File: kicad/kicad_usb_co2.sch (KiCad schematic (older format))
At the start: 7 parts, among them SW1 SW_SPDT, SW2 SW_SPDT, U1 MH-Z19B, U2 SeeeduinoXIAO, U3 MH-Z14A

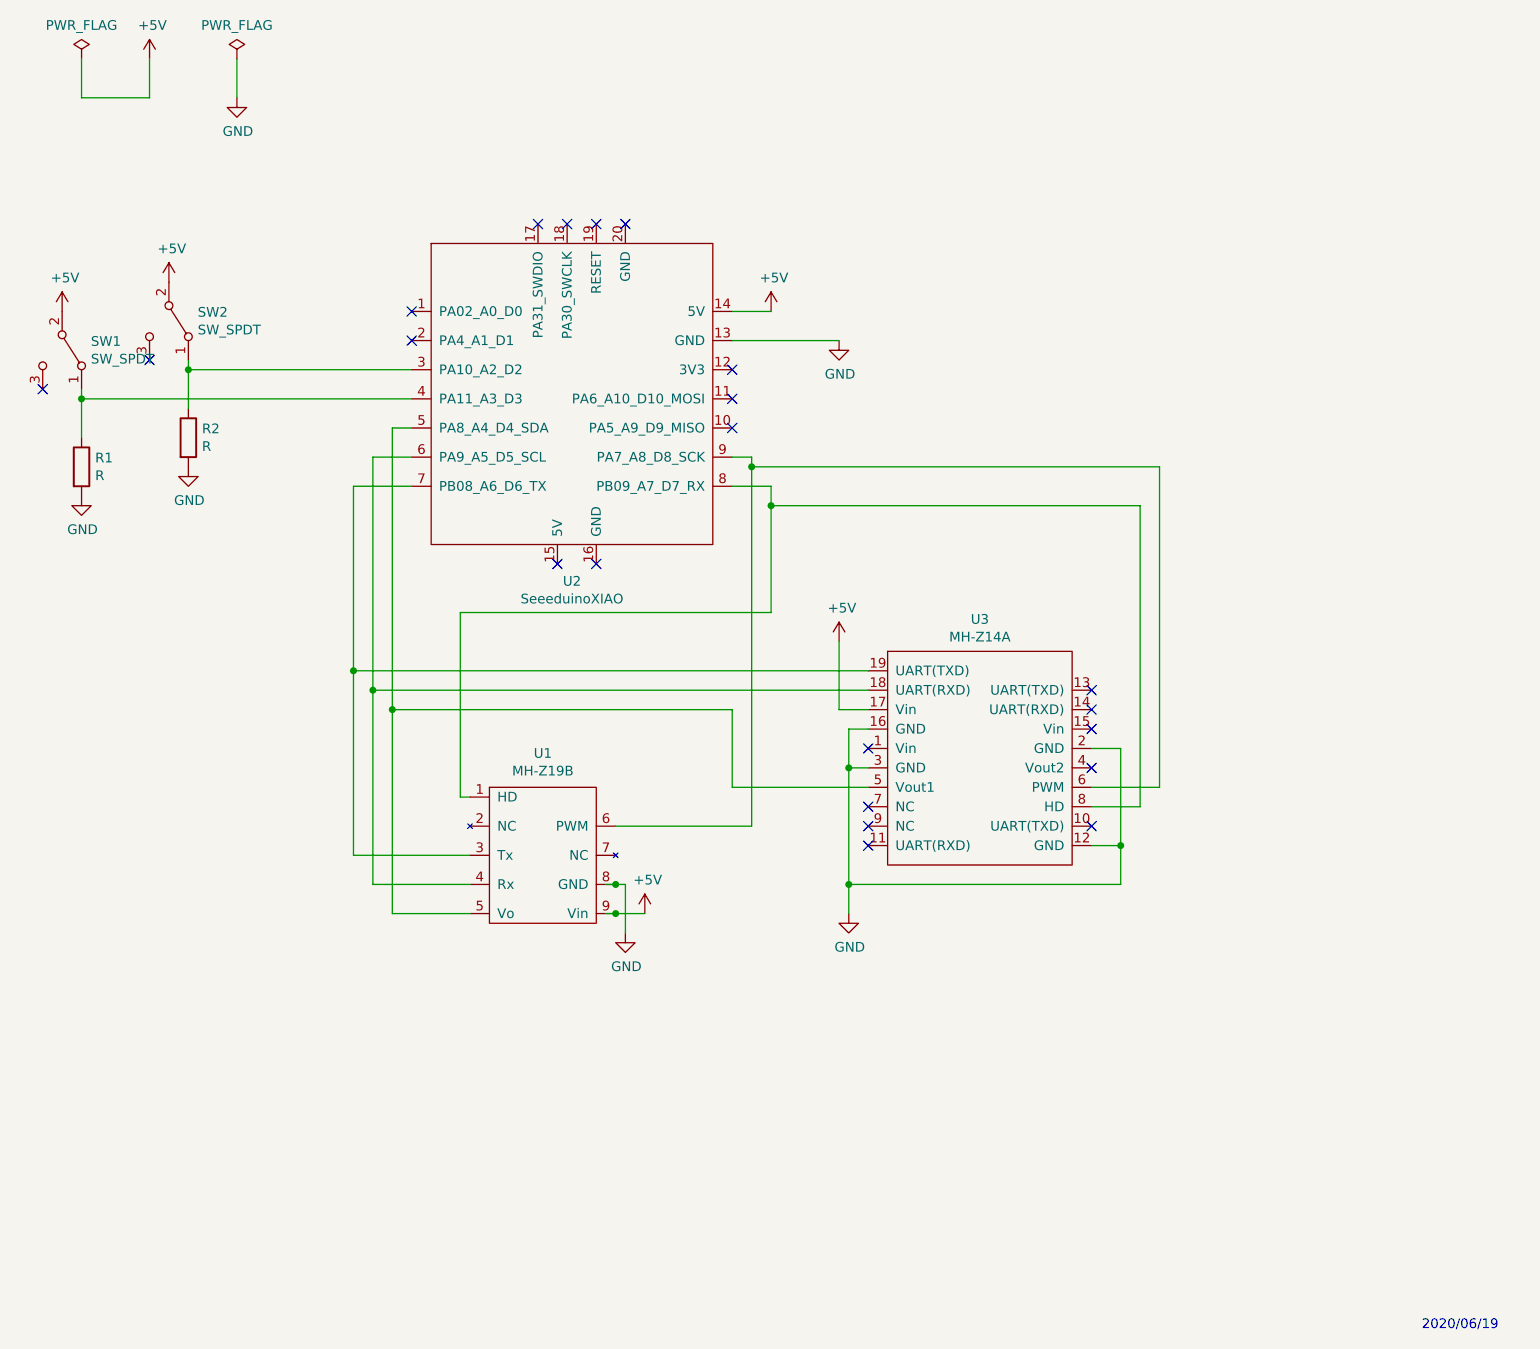
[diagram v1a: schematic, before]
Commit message: XIAOのピンをすべてピンヘッダに出した
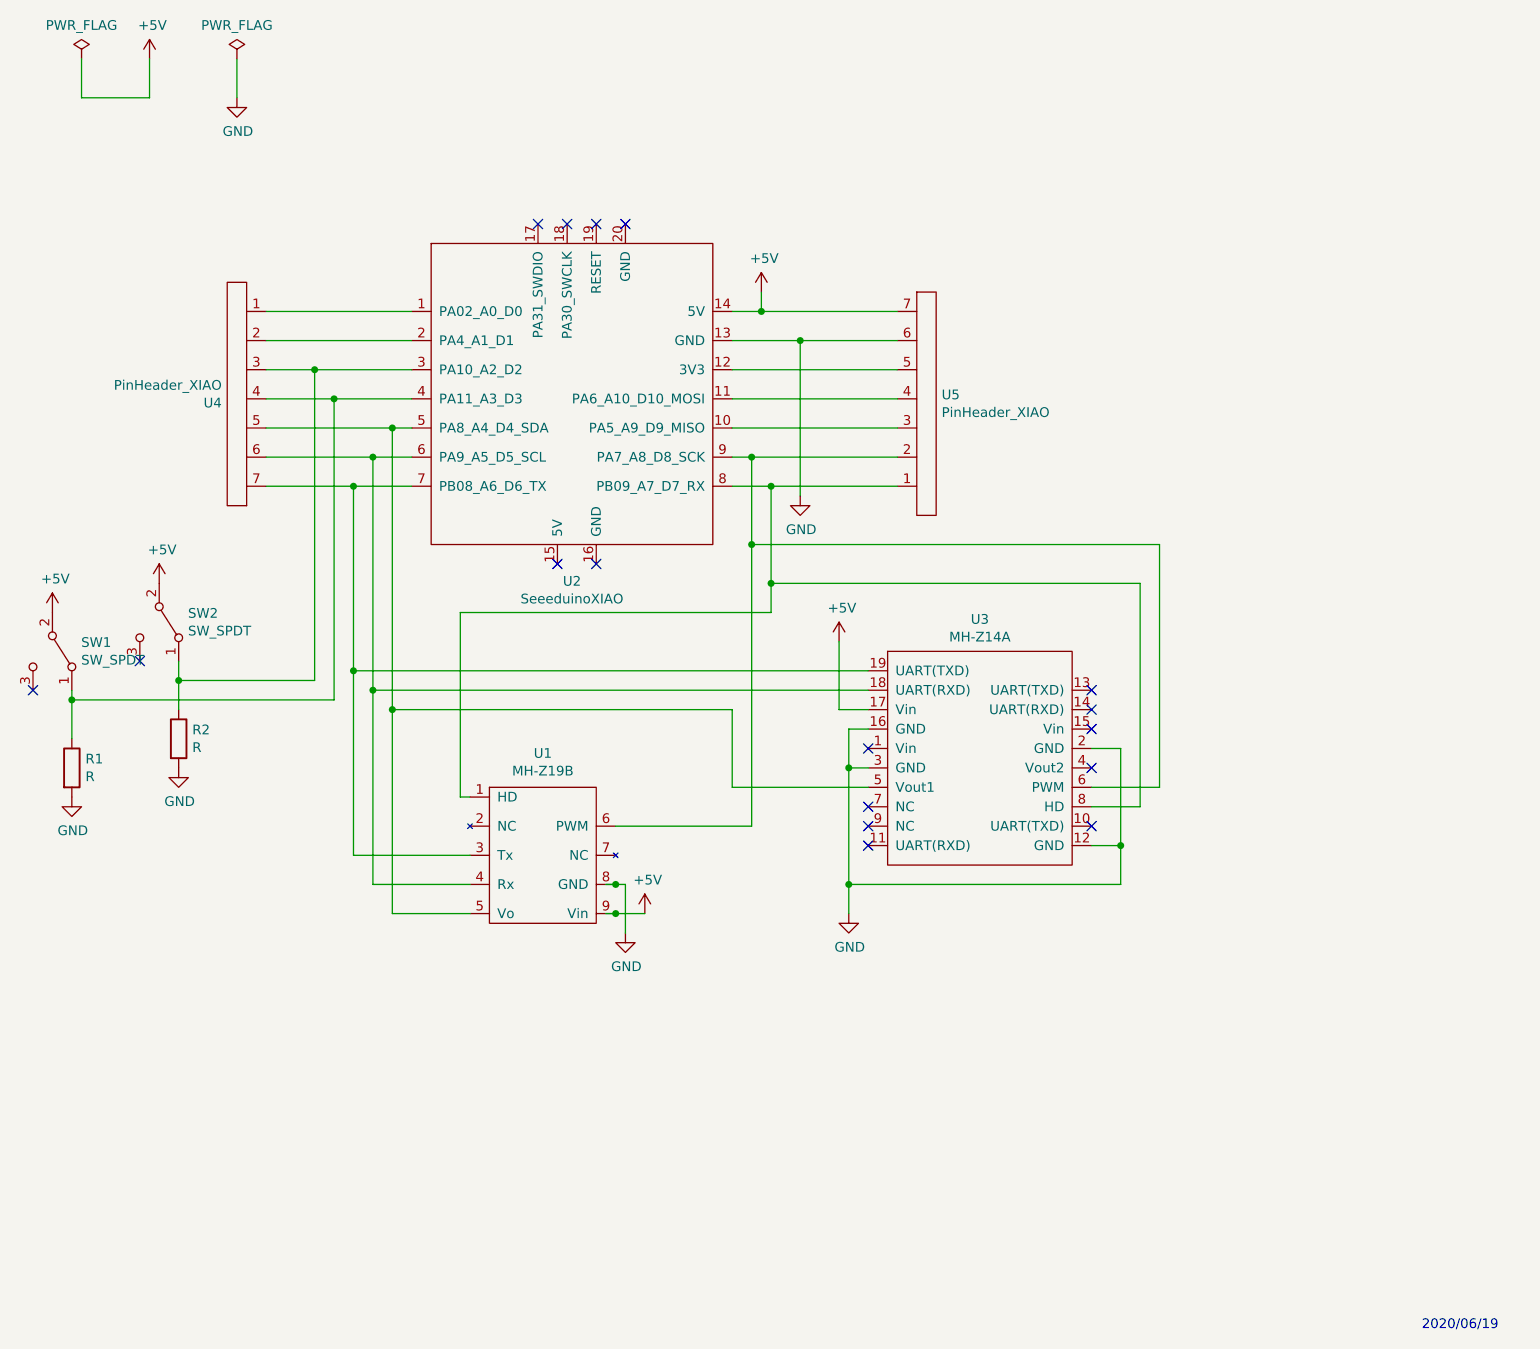
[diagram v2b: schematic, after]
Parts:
- added U4, U5: PinHeader_XIAO, symbol kicad_mylib:PinHeader_XIAO
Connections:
- wire segments 62 -> 82
- no-connect marks 22 -> 17
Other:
- moved on the sheet: R1, R2, SW1, SW2
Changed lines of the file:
@@
 L power:GND #PWR0103
 U 1 1 5EECC900
-P 5100 2550
-F 0 "#PWR0103" H 5100 2300 50  0001 C CNN
-F 1 "GND" H 5105 2377 50  0000 C CNN
-F 2 "" H 5100 2550 50  0001 C CNN
-F 3 "" H 5100 2550 50  0001 C CNN
-	1    5100 2550
-	1    0    0    -1
-$EndComp
-Wire Wire Line
-	4550 2550 5100 2550
-$Comp
-L Device:R R1
-U 1 1 5EEDD236
-P 1200 3200
-F 0 "R1" H 1270 3246 50  0000 L CNN
-F 1 "R" H 1270 3155 50  0000 L CNN
-F 2 "Resistor_THT:R_Axial_DIN0207_L6.3mm_D2.5mm_P10.16mm_Horizontal" V 1130 3200 50  0001 C CNN
-F 3 "~" H 1200 3200 50  0001 C CNN
-	1    1200 3200
-	1    0    0    -1
-$EndComp
-$Comp
-L Device:R R2
-U 1 1 5EEDD7FF
-P 1750 3050
-F 0 "R2" H 1820 3096 50  0000 L CNN
-F 1 "R" H 1820 3005 50  0000 L CNN
-F 2 "Resistor_THT:R_Axial_DIN0207_L6.3mm_D2.5mm_P10.16mm_Horizontal" V 1680 3050 50  0001 C CNN
-F 3 "~" H 1750 3050 50  0001 C CNN
-	1    1750 3050
-	1    0    0    -1
-$EndComp
-$Comp
-L power:GND #PWR0105
-U 1 1 5EEDDA13
-P 1200 3350
-F 0 "#PWR0105" H 1200 3100 50  0001 C CNN
-F 1 "GND" H 1205 3177 50  0000 C CNN
-F 2 "" H 1200 3350 50  0001 C CNN
-F 3 "" H 1200 3350 50  0001 C CNN
-	1    1200 3350
-	1    0    0    -1
-$EndComp
-$Comp
-L power:GND #PWR0106
-U 1 1 5EEDDEAF
-P 1750 3200
-F 0 "#PWR0106" H 1750 2950 50  0001 C CNN
-F 1 "GND" H 1755 3027 50  0000 C CNN
-F 2 "" H 1750 3200 50  0001 C CNN
-F 3 "" H 1750 3200 50  0001 C CNN
-	1    1750 3200
-	1    0    0    -1
-$EndComp
-NoConn ~ 4550 2700
-NoConn ~ 4550 3000
+P 4900 3350
+F 0 "#PWR0103" H 4900 3100 50  0001 C CNN
+F 1 "GND" H 4905 3177 50  0000 C CNN
+F 2 "" H 4900 3350 50  0001 C CNN
+F 3 "" H 4900 3350 50  0001 C CNN
+	1    4900 3350
+	1    0    0    -1
+$EndComp
 NoConn ~ 4000 1950
 NoConn ~ 3850 1950
@@
 	1    0    0    -1
 $EndComp
-NoConn ~ 4550 2850
-Wire Wire Line
-	4750 2400 4550 2400
-$Comp
-L Switch:SW_SPDT SW2
-U 1 1 5F3D6A6E
-P 1650 2450
-F 0 "SW2" V 1604 2598 50  0000 L CNN
-F 1 "SW_SPDT" V 1695 2598 50  0000 L CNN
-F 2 "Mylib:SW_SLIDE_sengoku" H 1650 2450 50  0001 C CNN
-F 3 "~" H 1650 2450 50  0001 C CNN
-	1    1650 2450
-	0    1    1    0
-$EndComp
-NoConn ~ 2900 2400
-NoConn ~ 2900 2550
-NoConn ~ 1550 2650
-NoConn ~ 1000 2800
 Wire Wire Line
 	4000 5350 4000 5600
@@
 L power:+5V #PWR02
 U 1 1 5F8A2F84
-P 4750 2400
-F 0 "#PWR02" H 4750 2250 50  0001 C CNN
-F 1 "+5V" H 4765 2573 50  0000 C CNN
-F 2 "" H 4750 2400 50  0001 C CNN
-F 3 "" H 4750 2400 50  0001 C CNN
-	1    4750 2400
-	1    0    0    -1
-$EndComp
-$Comp
-L Switch:SW_SPDT SW1
-U 1 1 5F3D76FF
-P 1100 2600
-F 0 "SW1" V 1054 2748 50  0000 L CNN
-F 1 "SW_SPDT" V 1145 2748 50  0000 L CNN
-F 2 "Mylib:SW_SLIDE_sengoku" H 1100 2600 50  0001 C CNN
-F 3 "~" H 1100 2600 50  0001 C CNN
-	1    1100 2600
-	0    1    1    0
-$EndComp
-$Comp
-L power:+5V #PWR03
-U 1 1 5F8A6AAD
-P 1100 2400
-F 0 "#PWR03" H 1100 2250 50  0001 C CNN
-F 1 "+5V" H 1115 2573 50  0000 C CNN
-F 2 "" H 1100 2400 50  0001 C CNN
-F 3 "" H 1100 2400 50  0001 C CNN
-	1    1100 2400
-	1    0    0    -1
-$EndComp
-$Comp
-L power:+5V #PWR04
-U 1 1 5F8A7015
-P 1650 2250
-F 0 "#PWR04" H 1650 2100 50  0001 C CNN
-F 1 "+5V" H 1665 2423 50  0000 C CNN
-F 2 "" H 1650 2250 50  0001 C CNN
-F 3 "" H 1650 2250 50  0001 C CNN
-	1    1650 2250
+P 4700 2300
+F 0 "#PWR02" H 4700 2150 50  0001 C CNN
+F 1 "+5V" H 4715 2473 50  0000 C CNN
+F 2 "" H 4700 2300 50  0001 C CNN
+F 3 "" H 4700 2300 50  0001 C CNN
+	1    4700 2300
 	1    0    0    -1
 $EndComp
@@
 	3900 5350 3950 5350
 Wire Wire Line
-	4750 3300 4750 3400
-Wire Wire Line
 	4650 5050 3950 5050
 Wire Wire Line
@@
 	3150 3950 3150 4900
 Wire Wire Line
-	4650 3150 4650 3200
-Wire Wire Line
 	5250 4250 2600 4250
 Connection ~ 2600 4250
@@
 	6400 4950 6650 4950
 Wire Wire Line
-	6650 4950 6650 3400
-Wire Wire Line
-	6650 3400 4750 3400
-Connection ~ 4750 3400
-Wire Wire Line
-	4750 3400 4750 3950
-Wire Wire Line
 	6400 4850 6750 4850
-Wire Wire Line
-	6750 4850 6750 3200
-Wire Wire Line
-	6750 3200 4650 3200
-Connection ~ 4650 3200
-Wire Wire Line
-	4650 3200 4650 5050
 NoConn ~ 6400 4350
 NoConn ~ 6400 4450
@@
 NoConn ~ 5250 4950
 NoConn ~ 5250 5150
-Connection ~ 1200 2850
-Wire Wire Line
-	1200 2850 1200 3050
-Wire Wire Line
-	1200 2800 1200 2850
-Connection ~ 1750 2700
-Wire Wire Line
-	1750 2700 1750 2900
-Wire Wire Line
-	1750 2650 1750 2700
-Wire Wire Line
-	2900 2850 1200 2850
-Wire Wire Line
-	2900 2700 1750 2700
+$Comp
+L Device:R R1
+U 1 1 5EEDD236
+P 1150 4750
+F 0 "R1" H 1220 4796 50  0000 L CNN
+F 1 "R" H 1220 4705 50  0000 L CNN
+F 2 "Resistor_THT:R_Axial_DIN0207_L6.3mm_D2.5mm_P10.16mm_Horizontal" V 1080 4750 50  0001 C CNN
+F 3 "~" H 1150 4750 50  0001 C CNN
+	1    1150 4750
+	1    0    0    -1
+$EndComp
+$Comp
+L Device:R R2
+U 1 1 5EEDD7FF
+P 1700 4600
+F 0 "R2" H 1770 4646 50  0000 L CNN
+F 1 "R" H 1770 4555 50  0000 L CNN
+F 2 "Resistor_THT:R_Axial_DIN0207_L6.3mm_D2.5mm_P10.16mm_Horizontal" V 1630 4600 50  0001 C CNN
+F 3 "~" H 1700 4600 50  0001 C CNN
+	1    1700 4600
+	1    0    0    -1
+$EndComp
+$Comp
+L power:GND #PWR0105
+U 1 1 5EEDDA13
+P 1150 4900
+F 0 "#PWR0105" H 1150 4650 50  0001 C CNN
+F 1 "GND" H 1155 4727 50  0000 C CNN
+F 2 "" H 1150 4900 50  0001 C CNN
+F 3 "" H 1150 4900 50  0001 C CNN
+	1    1150 4900
+	1    0    0    -1
+$EndComp
+$Comp
+L power:GND #PWR0106
+U 1 1 5EEDDEAF
+P 1700 4750
+F 0 "#PWR0106" H 1700 4500 50  0001 C CNN
+F 1 "GND" H 1705 4577 50  0000 C CNN
+F 2 "" H 1700 4750 50  0001 C CNN
+F 3 "" H 1700 4750 50  0001 C CNN
+	1    1700 4750
+	1    0    0    -1
+$EndComp
+$Comp
+L Switch:SW_SPDT SW2
+U 1 1 5F3D6A6E
+P 1600 4000
+F 0 "SW2" V 1554 4148 50  0000 L CNN
+F 1 "SW_SPDT" V 1645 4148 50  0000 L CNN
+F 2 "Mylib:SW_SLIDE_sengoku" H 1600 4000 50  0001 C CNN
+F 3 "~" H 1600 4000 50  0001 C CNN
+	1    1600 4000
+	0    1    1    0
+$EndComp
+NoConn ~ 1500 4200
+NoConn ~ 950  4350
+$Comp
+L Switch:SW_SPDT SW1
+U 1 1 5F3D76FF
+P 1050 4150
+F 0 "SW1" V 1004 4298 50  0000 L CNN
+F 1 "SW_SPDT" V 1095 4298 50  0000 L CNN
+F 2 "Mylib:SW_SLIDE_sengoku" H 1050 4150 50  0001 C CNN
+F 3 "~" H 1050 4150 50  0001 C CNN
+	1    1050 4150
+	0    1    1    0
+$EndComp
+$Comp
+L power:+5V #PWR03
+U 1 1 5F8A6AAD
+P 1050 3950
+F 0 "#PWR03" H 1050 3800 50  0001 C CNN
+F 1 "+5V" H 1065 4123 50  0000 C CNN
+F 2 "" H 1050 3950 50  0001 C CNN
+F 3 "" H 1050 3950 50  0001 C CNN
+	1    1050 3950
+	1    0    0    -1
+$EndComp
+$Comp
+L power:+5V #PWR04
+U 1 1 5F8A7015
+P 1600 3800
+F 0 "#PWR04" H 1600 3650 50  0001 C CNN
+F 1 "+5V" H 1615 3973 50  0000 C CNN
+F 2 "" H 1600 3800 50  0001 C CNN
+F 3 "" H 1600 3800 50  0001 C CNN
+	1    1600 3800
+	1    0    0    -1
+$EndComp
+Wire Wire Line
+	1150 4350 1150 4400
+Wire Wire Line
+	1700 4200 1700 4300
+$Comp
+L kicad_mylib:PinHeader_XIAO U4
+U 1 1 5F9B9907
+P 2050 2250
+F 0 "U4" H 2178 2871 50  0000 L CNN
+F 1 "PinHeader_XIAO" H 2178 2780 50  0000 L CNN
+F 2 "" H 2100 3500 50  0001 C CNN
+F 3 "" H 2100 3500 50  0001 C CNN
+	1    2050 2250
+	-1   0    0    1
+$EndComp
+Wire Wire Line
+	2900 2400 2150 2400
+Wire Wire Line
+	2150 2550 2900 2550
+Wire Wire Line
+	2150 2700 2400 2700
+Wire Wire Line
+	2150 2850 2500 2850
+Wire Wire Line
+	2150 3000 2800 3000
+Connection ~ 2800 3000
+Wire Wire Line
+	2150 3150 2700 3150
+Connection ~ 2700 3150
+Wire Wire Line
+	2150 3300 2600 3300
+Connection ~ 2600 3300
+Wire Wire Line
+	2500 2850 2500 4400
+Wire Wire Line
+	2500 4400 1150 4400
+Connection ~ 2500 2850
+Wire Wire Line
+	2500 2850 2900 2850
+Connection ~ 1150 4400
+Wire Wire Line
+	1150 4400 1150 4600
+Wire Wire Line
+	2400 2700 2400 4300
+Wire Wire Line
+	2400 4300 1700 4300
+Connection ~ 2400 2700
+Wire Wire Line
+	2400 2700 2900 2700
+Connection ~ 1700 4300
+Wire Wire Line
+	1700 4300 1700 4450
+Wire Wire Line
+	6750 4850 6750 3600
+Wire Wire Line
+	6650 4950 6650 3800
+Wire Wire Line
+	6750 3600 4650 3600
+Wire Wire Line
+	6650 3800 4750 3800
+Connection ~ 4650 3600
+Wire Wire Line
+	4650 3600 4650 5050
+Connection ~ 4750 3800
+Wire Wire Line
+	4750 3800 4750 3950
+Wire Wire Line
+	4750 3300 4750 3800
+Wire Wire Line
+	4650 3150 4650 3600
+$Comp
+L kicad_mylib:PinHeader_XIAO U5
+U 1 1 5F9EC865
+P 5500 3450
+F 0 "U5" H 5628 4071 50  0000 L CNN
+F 1 "PinHeader_XIAO" H 5628 3980 50  0000 L CNN
+F 2 "" H 5550 4700 50  0001 C CNN
+F 3 "" H 5550 4700 50  0001 C CNN
+	1    5500 3450
+	1    0    0    -1
+$EndComp
+Wire Wire Line
+	5400 3300 4750 3300
+Connection ~ 4750 3300
+Wire Wire Line
+	4650 3150 5400 3150
+Connection ~ 4650 3150
+Wire Wire Line
+	5400 3000 4550 3000
+Wire Wire Line
+	4550 2850 5400 2850
+Wire Wire Line
+	5400 2700 4550 2700
+Wire Wire Line
+	4550 2550 4900 2550
+Wire Wire Line
+	4700 2300 4700 2400
+Wire Wire Line
+	4900 2550 4900 3350
+Connection ~ 4900 2550
+Wire Wire Line
+	4900 2550 5400 2550
+Connection ~ 4700 2400
+Wire Wire Line
+	4700 2400 4550 2400
+Wire Wire Line
+	4700 2400 5400 2400
 $EndSCHEMATC

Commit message: ピンヘッダのフットプリントが関連付いてなかった
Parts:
- U4, U5: footprint (none) -> kicad_mylib:PinHeader_XIAO
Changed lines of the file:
@@
 F 0 "U4" H 2178 2871 50  0000 L CNN
 F 1 "PinHeader_XIAO" H 2178 2780 50  0000 L CNN
-F 2 "" H 2100 3500 50  0001 C CNN
+F 2 "kicad_mylib:PinHeader_XIAO" H 2100 3500 50  0001 C CNN
 F 3 "" H 2100 3500 50  0001 C CNN
 	1    2050 2250
@@
 F 0 "U5" H 5628 4071 50  0000 L CNN
 F 1 "PinHeader_XIAO" H 5628 3980 50  0000 L CNN
-F 2 "" H 5550 4700 50  0001 C CNN
+F 2 "kicad_mylib:PinHeader_XIAO" H 5550 4700 50  0001 C CNN
 F 3 "" H 5550 4700 50  0001 C CNN
 	1    5500 3450

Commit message: 色々フットプリントが関連付いてなかった
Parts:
- SW1, SW2: footprint Mylib:SW_SLIDE_sengoku -> kicad_mylib:SW_SLIDE_sengoku
- U3: footprint My_lib:MH-Z14A -> kicad_mylib:MH-Z14A
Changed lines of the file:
@@
 F 0 "U3" H 5825 4515 50  0000 C CNN
 F 1 "MH-Z14A" H 5825 4424 50  0000 C CNN
-F 2 "My_lib:MH-Z14A" H 5400 4400 50  0001 C CNN
+F 2 "kicad_mylib:MH-Z14A" H 5400 4400 50  0001 C CNN
 F 3 "" H 5400 4400 50  0001 C CNN
 	1    5250 4250
@@
 F 0 "SW2" V 1554 4148 50  0000 L CNN
 F 1 "SW_SPDT" V 1645 4148 50  0000 L CNN
-F 2 "Mylib:SW_SLIDE_sengoku" H 1600 4000 50  0001 C CNN
+F 2 "kicad_mylib:SW_SLIDE_sengoku" H 1600 4000 50  0001 C CNN
 F 3 "~" H 1600 4000 50  0001 C CNN
 	1    1600 4000
@@
 F 0 "SW1" V 1004 4298 50  0000 L CNN
 F 1 "SW_SPDT" V 1095 4298 50  0000 L CNN
-F 2 "Mylib:SW_SLIDE_sengoku" H 1050 4150 50  0001 C CNN
+F 2 "kicad_mylib:SW_SLIDE_sengoku" H 1050 4150 50  0001 C CNN
 F 3 "~" H 1050 4150 50  0001 C CNN
 	1    1050 4150
